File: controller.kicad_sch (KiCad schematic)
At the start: 4 parts, among them SW1 RotaryEncoder_Switch, U6 ATmega328P-P, U7 DS3231MZ

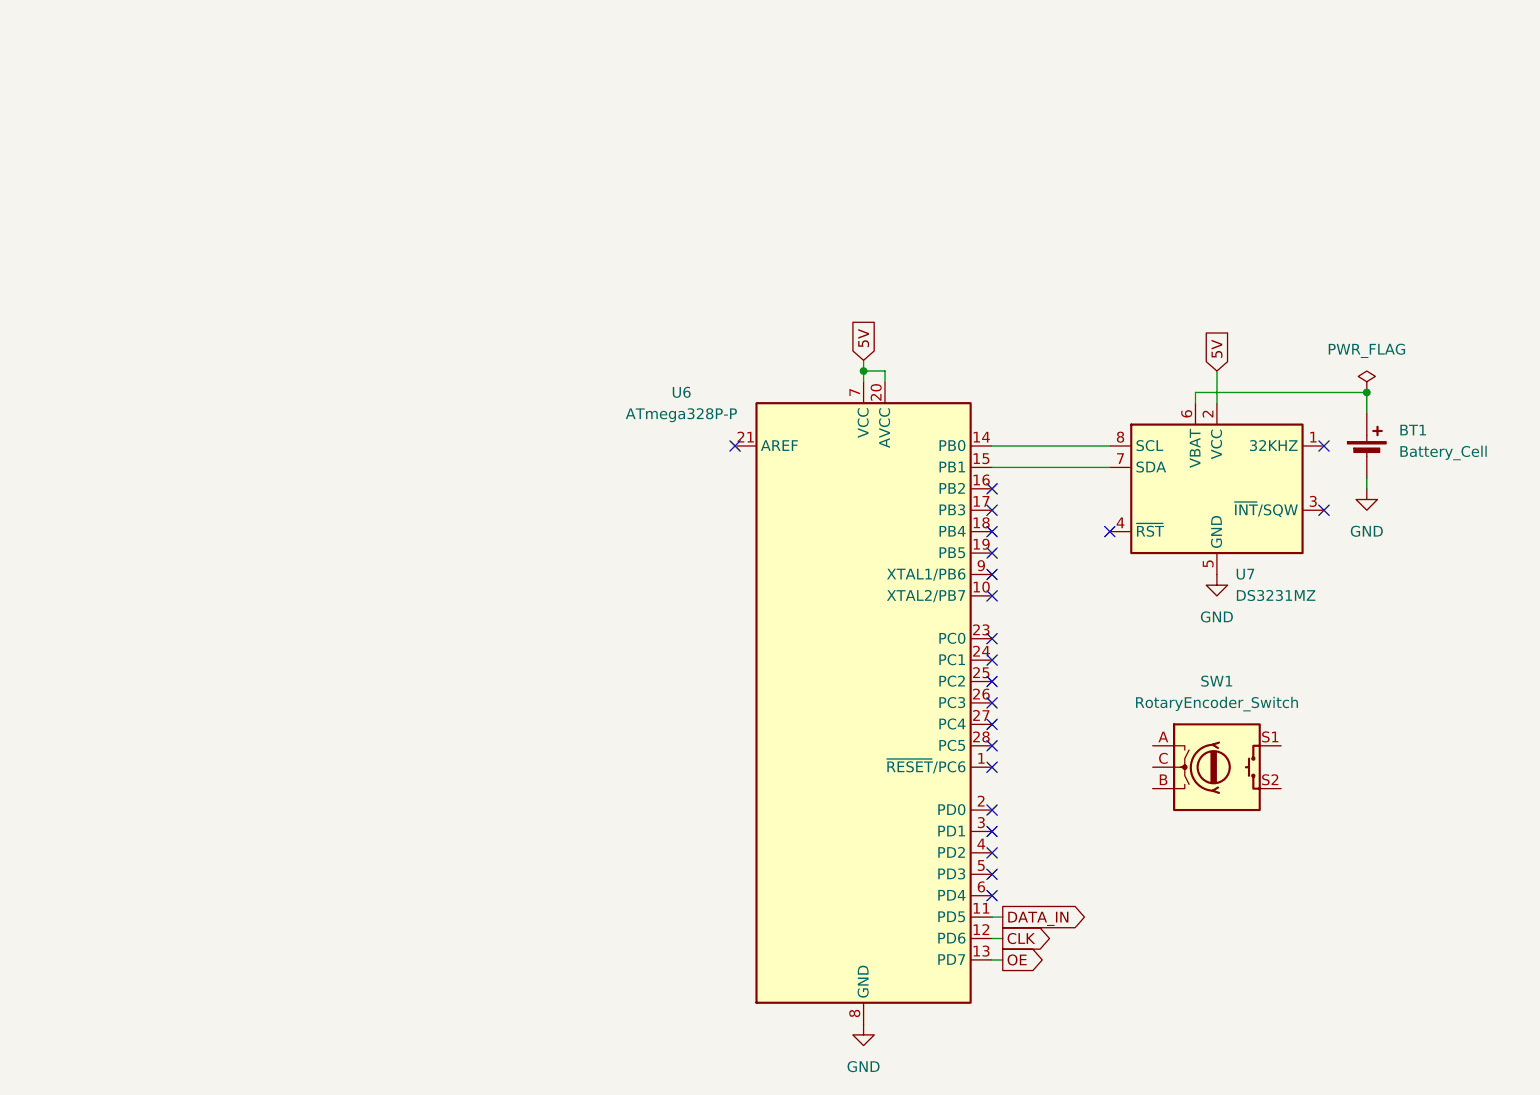
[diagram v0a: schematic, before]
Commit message: updated controller part
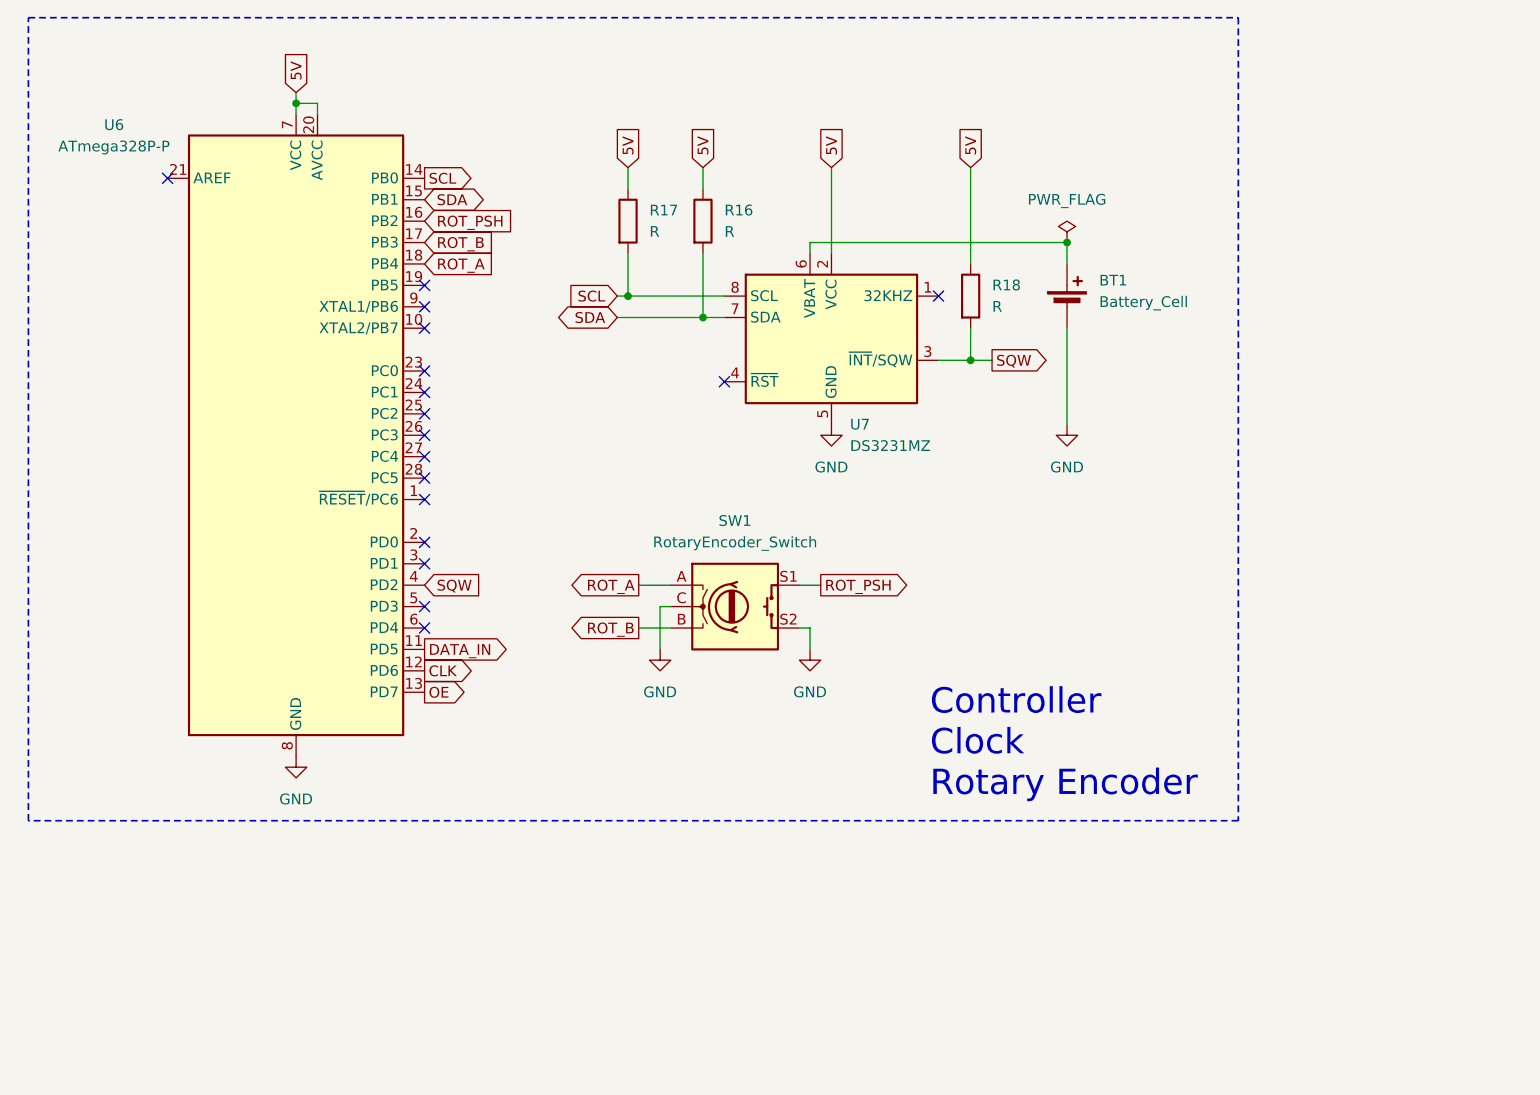
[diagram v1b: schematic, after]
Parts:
- added R16, R17, R18: R, symbol Device:R
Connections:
- net 5V: now also R16.1, R17.1, R18.1
- net GND: now also SW1.C, SW1.S2
- net SCL: now reaches U6.14 (PB0), U7.8 (SCL)
- net SCL: now also R17.2
- net SDA: now reaches U6.15 (PB1), U7.7 (SDA)
- net SDA: now also R16.2
- net ROT_PSH: now reaches U6.16 (PB2)
- net ROT_PSH: now also SW1.S1
- net ROT_B: now reaches U6.17 (PB3)
- net ROT_B: now also SW1.B
- net ROT_A: now reaches U6.18 (PB4)
- net ROT_A: now also SW1.A
- net SQW: now reaches U6.4 (PD2)
- net SQW: now also U7.3 (~{INT}/SQW), R18.2
- no-connect marks 22 -> 17
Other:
- note added: "Controller Clock Rotary Encoder"
- moved on the sheet: BT1, SW1, U6, U7

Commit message: added filter caps and rc debounce filter for rotary encoder
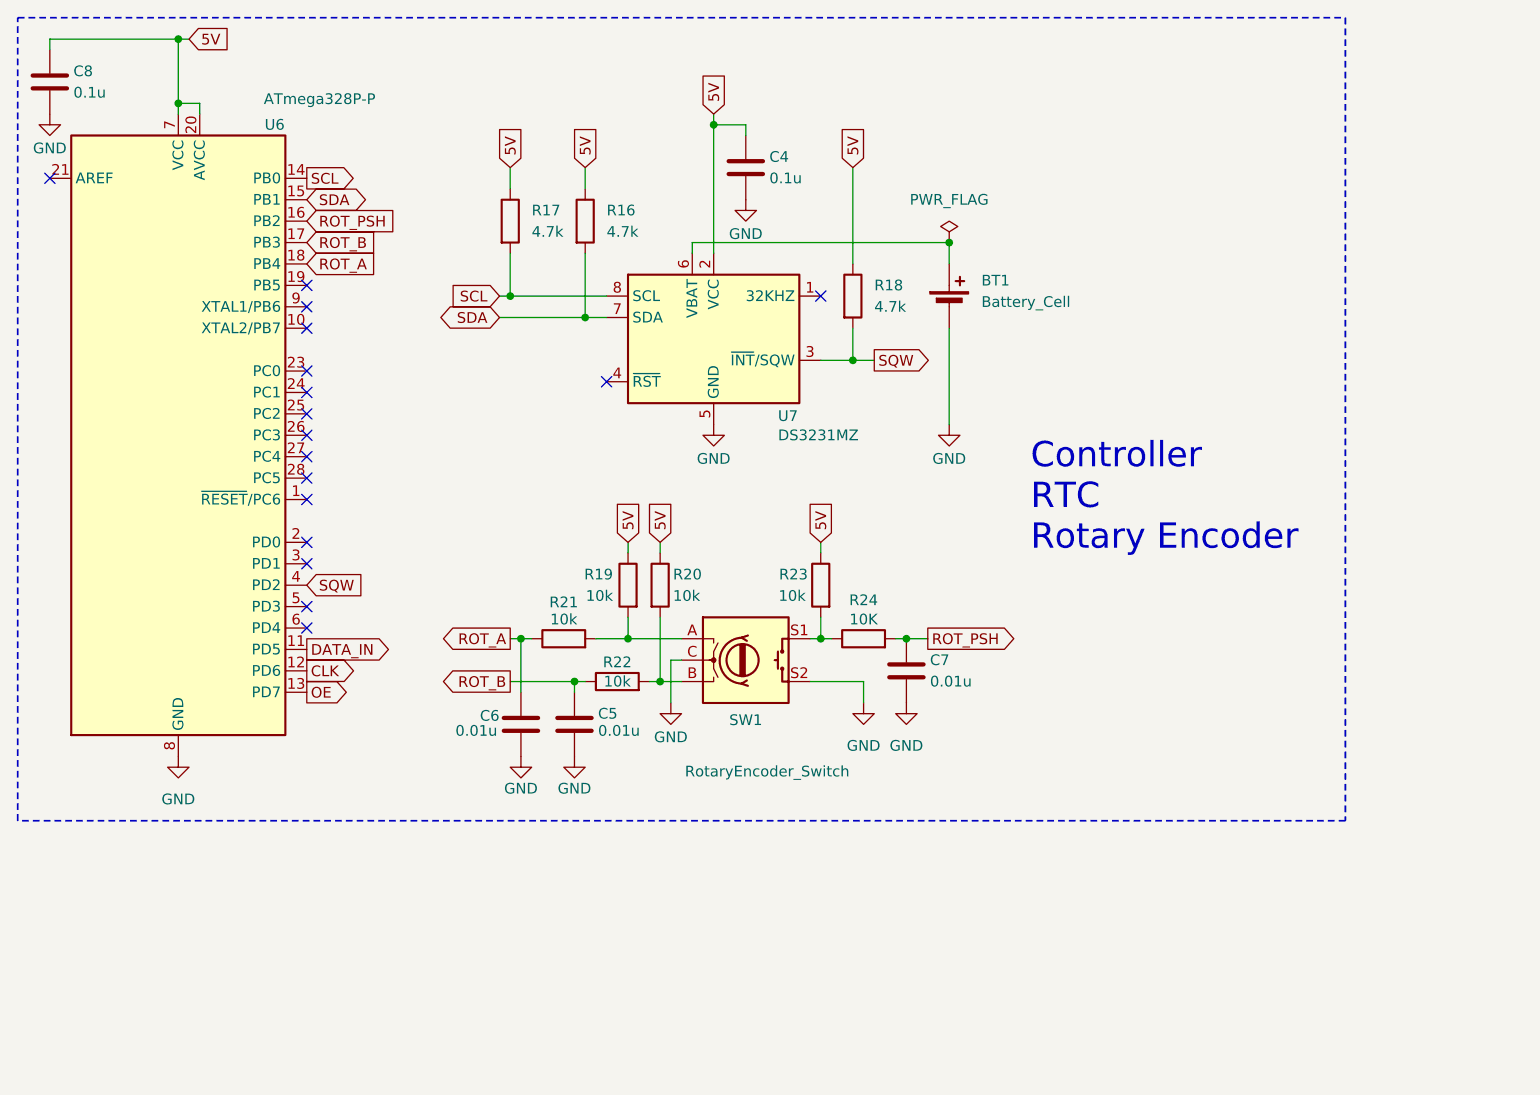
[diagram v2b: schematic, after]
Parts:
- added C4, C8: 0.1u, symbol Device:C
- added C5, C6, C7: 0.01u, symbol Device:C
- added R19, R20, R21, R22, R23: 10k, symbol Device:R
- added R24: 10K, symbol Device:R
- R16, R17, R18: value R -> 4.7k
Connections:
- net 5V: now also C4.1, C8.1, R19.1, R20.1, R23.1
- net GND: now also C4.2, C5.2, C6.2, C7.2, C8.2
- net ROT_A: now also C6.1, R21.1; no longer SW1.A
- net ROT_B: now also C5.1, R22.1; no longer SW1.B
- net ROT_PSH: now also C7.1, R24.2; no longer SW1.S1
- new net: R19.2, R21.2, SW1.A
- new net: R20.2, R22.2, SW1.B
- new net: R23.2, R24.1, SW1.S1
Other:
- note added: "Controller RTC Rotary Encoder"
- note removed: "Controller Clock Rotary Encoder"
- moved on the sheet: BT1, R16, R17, R18, SW1, U6, U7
